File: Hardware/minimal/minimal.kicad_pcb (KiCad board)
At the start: 4 copper layers, 48 x 35 mm, 96 parts, among them J101 USB_C_Receptacle_USB2.0_16P, J301 AudioJack3_SwitchTR, J302 AudioJack3_SwitchTR, J303 AudioJack4, SW101 SW_SPST, U101 KTM1331TD-ST3, U102 USBLC6-2P6, U103 TLV76733DRVx, U104 TLV76733DRVx, U301 OPA2323, U302 TAC5112, U401 APS6404L-3SQRx-ZR, U402 RP2354A, Y401 ABM8-272-T3

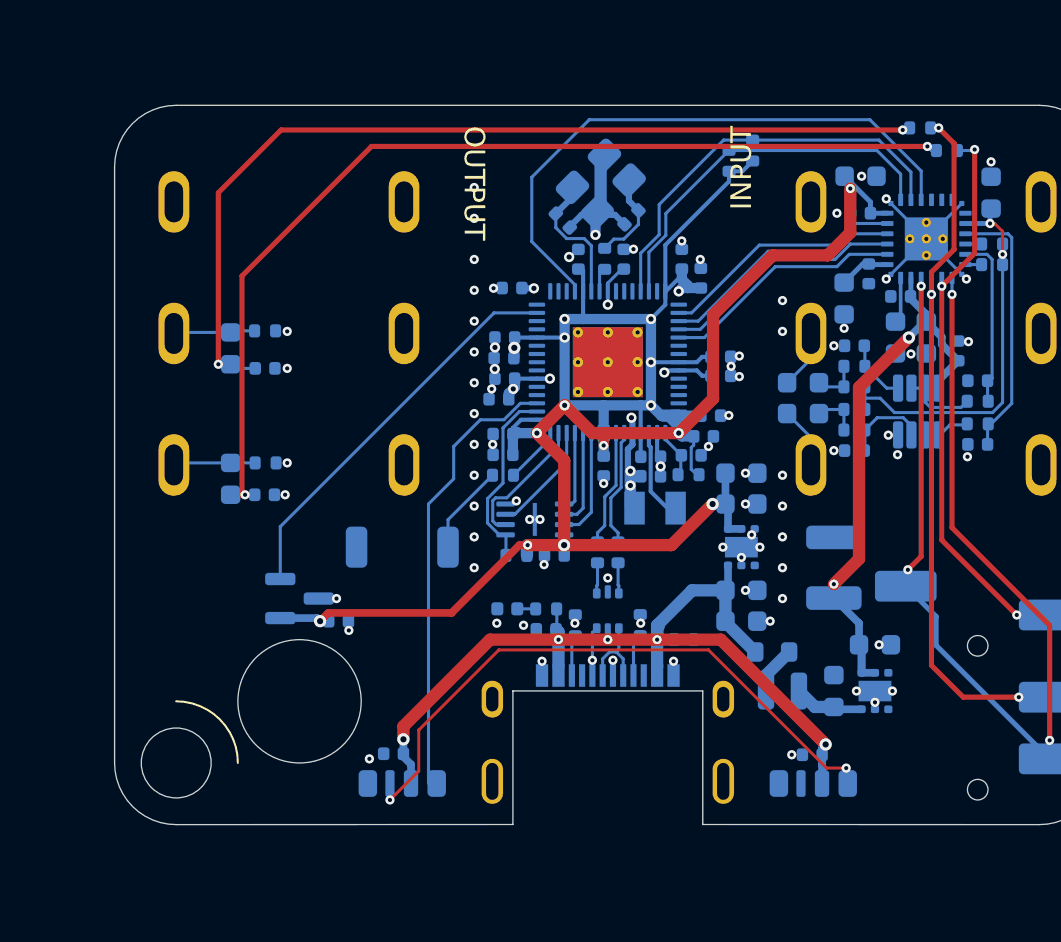
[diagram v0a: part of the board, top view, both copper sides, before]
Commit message: Update the minimal board with a nRF54L10 BLE chip
Let's see how this works.  It needs more sanity checking, but looks like
it might be workable, and it fits under the output jack which was mostly
empty space before.

The rp2354 still acts as the i2s master - now for both the TAC5112 and
the nRF54.  It also will act as the SWD programmer for the new Nordic
Semi chip.  So all programming still happens over the USB-C port, it's
just that you first need to teach the rp2354 how to program the nRF54.

That's probably a whole separate firmware part where the rp2354
temporarily just acts as a SWD programmer before it goes back to being a
guitar pedal.

The firmware side will be "interesting".  I've done a nRF52840 chip
before, and didn't exactly enjoy the strange Nordic SDK.  And the nRF54
SDK is very different with either a Zephyr model or a bare metal option
that looks more like the traditional one.  But it looks like if I want
to do BLE audio, I will need to use that Zephyr one.

That's a problem for another day.  But I have SWD, an UART, and a
separate set of i2s pins wired up to talk to the nRF54, so it should all
be just a small matter of programming.  If the hardware works.

Signed-off-by: Linus Torvalds <torvalds@linux-foundation.org>
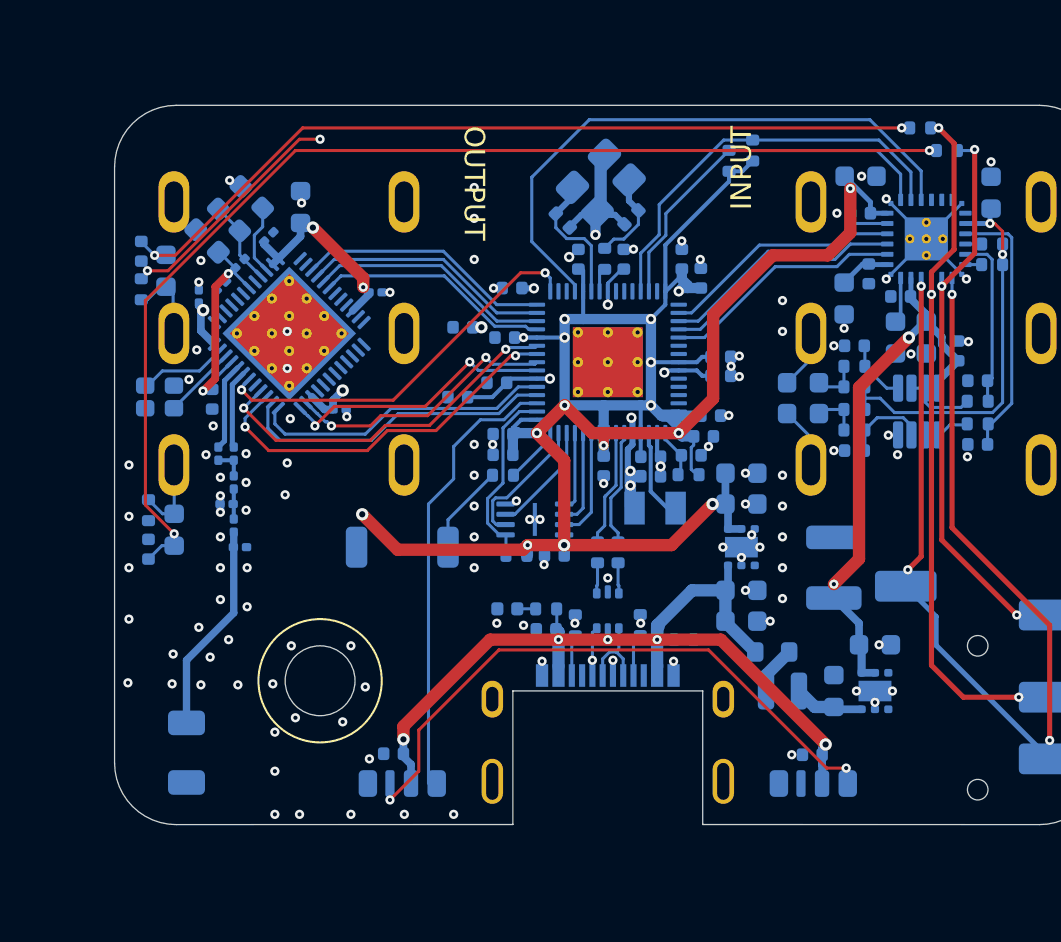
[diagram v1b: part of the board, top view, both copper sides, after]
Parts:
- removed C101: 0.1uF, Capacitor_SMD:C_0402_1005Metric
- removed U101: KTM1331TD-ST3, Package_TO_SOT_SMD:SOT-23
- added AE501: 2.4GHz, RF_Antenna:Johanson_2450AT18x100, B.Cu at (79.5, 131.5)
- added C501: 1.5pF, Capacitor_SMD:C_0201_0603Metric, B.Cu at (81.0, 117.0)
- added C502: 2.0pF, Capacitor_SMD:C_0201_0603Metric, B.Cu at (81.5, 119.4)
- added C503: 0.3pF, Capacitor_SMD:C_0201_0603Metric, B.Cu at (82.1, 121.5)
- added C504: 0.1uF, Capacitor_SMD:C_0201_0603Metric, B.Cu at (88.7, 109.1)
- added C505: 0.1uF, Capacitor_SMD:C_0201_0603Metric, B.Cu at (80.1, 109.3)
- added C506: 0.1uF, Capacitor_SMD:C_0201_0603Metric, B.Cu at (87.0, 114.8)
- added C507: 0.1uF, Capacitor_SMD:C_0201_0603Metric, B.Cu at (83.5, 106.4)
- added C508: 10uF, Capacitor_SMD:C_0603_1608Metric, B.Cu at (85.0, 105.0)
- added C509: 2.2uF, Capacitor_SMD:C_0603_1608Metric, B.Cu at (81.6, 104.5)
- added C510: 2.2uF, Capacitor_SMD:C_0603_1608Metric, B.Cu at (80.5, 106.6)
- added C511: 2.2nF, Capacitor_SMD:C_0402_1005Metric, B.Cu at (80.8, 114.3)
- added C512: 10nF, Capacitor_SMD:C_0201_0603Metric, B.Cu at (81.2, 108.8)
- added FB501: 120Ω, Inductor_SMD:L_0201_0603Metric, B.Cu at (82.1, 107.7)
- added L501: 4.7uH, Inductor_SMD:L_0603_1608Metric, B.Cu at (82.7, 105.5)
- added L502: 2.7nH, Inductor_SMD:L_0201_0603Metric, B.Cu at (81.8, 117.0)
- added L503: 3.5nH, Inductor_SMD:L_0201_0603Metric, B.Cu at (81.8, 118.3)
- added L504: 3.5nH, Inductor_SMD:L_0201_0603Metric, B.Cu at (81.8, 120.5)
- added U501: NRF54L10-QFAA-R7, Package_DFN_QFN:QFN-48-1EP_6x6mm_P0.4mm_EP4.6x4.6mm_ThermalVias, B.Cu at (84.5, 111.1)
- added Y501: 32MHz, Crystal:Crystal_SMD_2016-4Pin_2.0x1.6mm, B.Cu at (78.2, 114.2)
- moved C308 8.29 mm to (77.3, 107.1), turned to 90 degrees
- moved R308 6.36 mm to (77.3, 109.0), turned to 90 degrees
- moved C302 6.24 mm to (77.7, 121.6), turned to -90 degrees
- moved R302 6.15 mm to (77.7, 119.7), turned to -90 degrees
- moved C309 4.92 mm to (78.5, 108.0), turned to -90 degrees
- moved C305 3.70 mm to (78.9, 120.7)
- moved C414 2.50 mm to (93.0, 110.8)
- moved C403 2.00 mm to (92.7, 114.2)
- moved C407 0.44 mm to (94.6, 113.5)
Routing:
- net +3V3: track 146.2 -> 177.2 mm, vias 17 -> 22
- net /RP2354/GPIO12: track 0.00 -> 19.2 mm, vias 0 -> 2
- net /RP2354/GPIO6: track 0.00 -> 18.5 mm, vias 0 -> 2
- net /RP2354/GPIO7: track 0.00 -> 18.0 mm, vias 0 -> 2
- net GND: track 17.9 -> 34.0 mm, vias 82 -> 121
- net /RP2354/GPIO2: track 0.00 -> 15.6 mm
- net /RP2354/GPIO3: track 0.00 -> 14.7 mm
- net /RP2354/GPIO5: track 0.00 -> 13.3 mm, vias 0 -> 2
- net /RP2354/GPIO4: track 0.00 -> 13.3 mm, vias 0 -> 2
- net /RP2354/GPIO11: track 0.00 -> 12.4 mm
- net /RP2354/GPIO9: track 0.00 -> 11.8 mm
- net /nRF54L10/DECA: track 0.00 -> 11.7 mm, vias 0 -> 2
- net /RP2354/GPIO8: track 0.00 -> 11.4 mm
- net Net-(AE501-FEED): track 0.00 -> 10.2 mm
- net /RP2354/GPIO10: track 19.3 -> 12.1 mm
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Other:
- outline, holes or cut-outs redrawn
